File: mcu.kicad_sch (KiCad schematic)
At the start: 65 parts, among them J1 USB_C, P20 HEADER-2x11, P22 HEADER-2x13, P26 LPC_JTAG, P28 HEADER-2x11, SW1 SWITCH, SW2 SWITCH, U15 TVS_USB, U20 W25Q80, U23 LPC4330FET180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

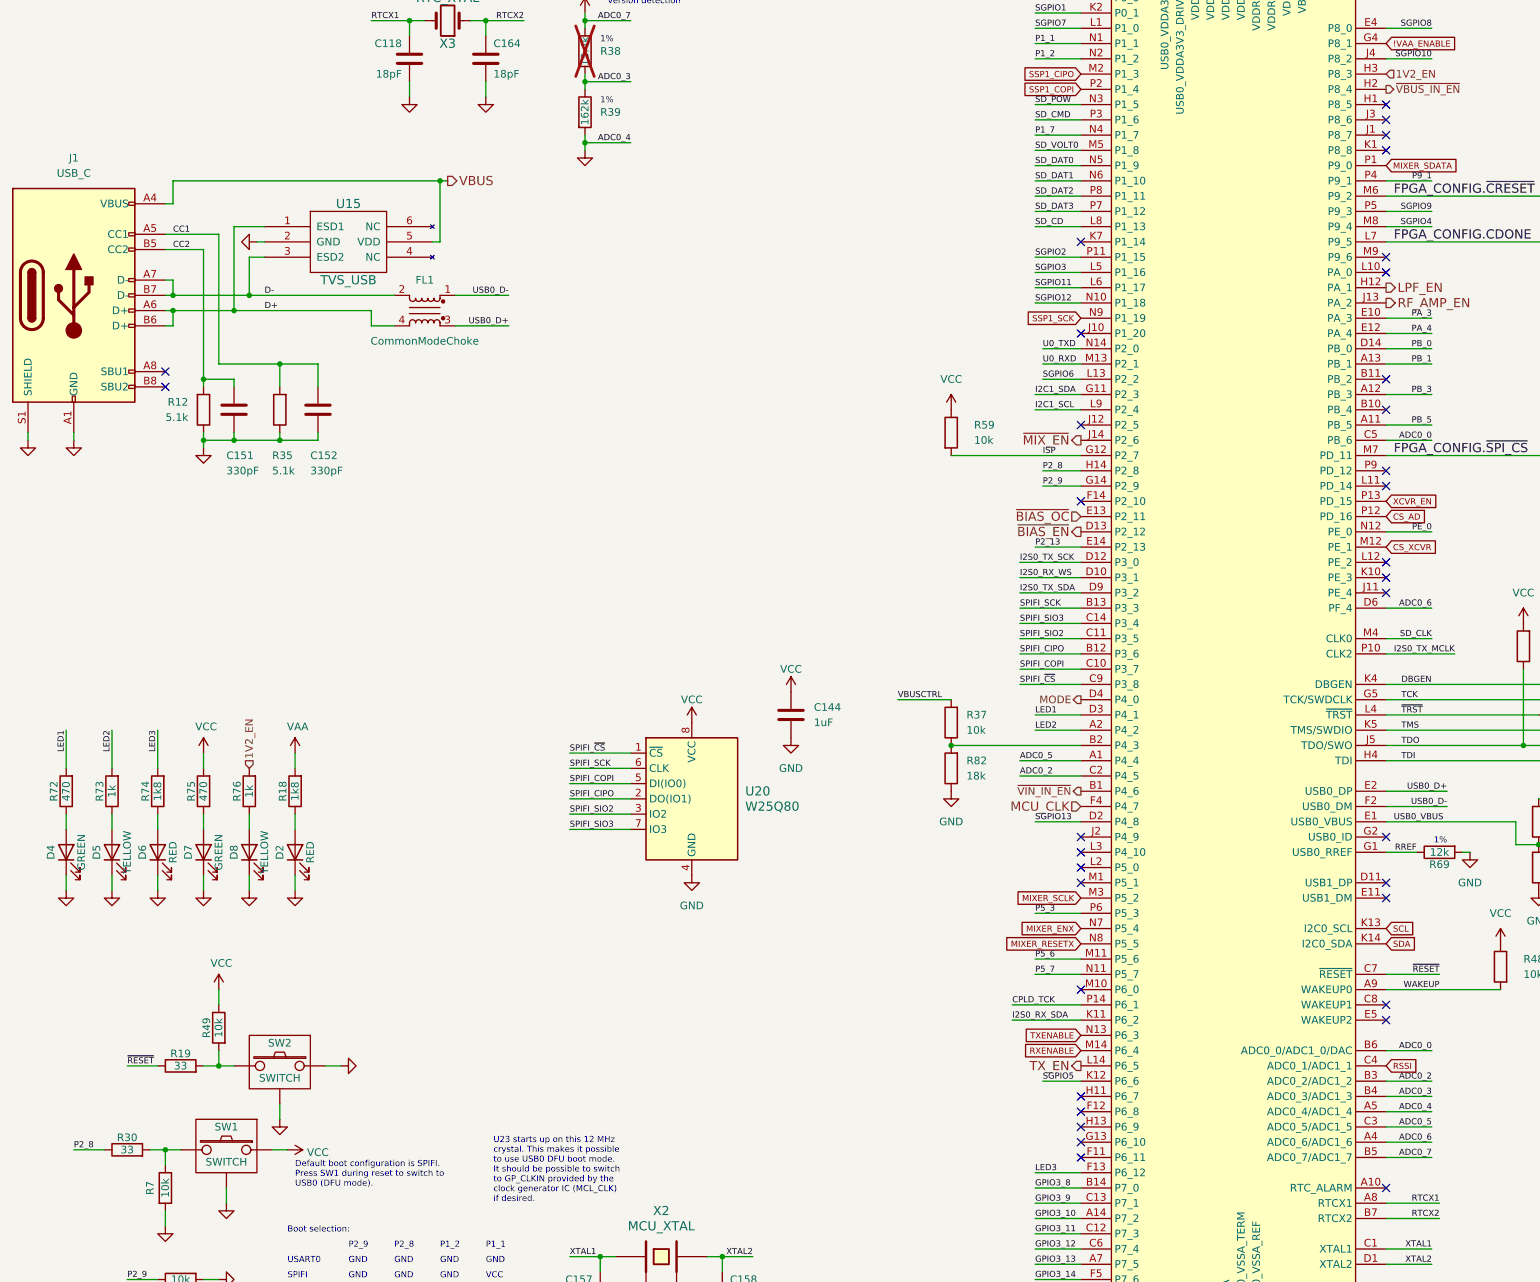
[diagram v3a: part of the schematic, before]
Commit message: Ensure LEDs can remain off in low power modes
- Change "3V3" LED to "MCU" LED4
- Change "1V2" LED to "FPGA" on 3V3FPGA
- Make LED control signals active-low
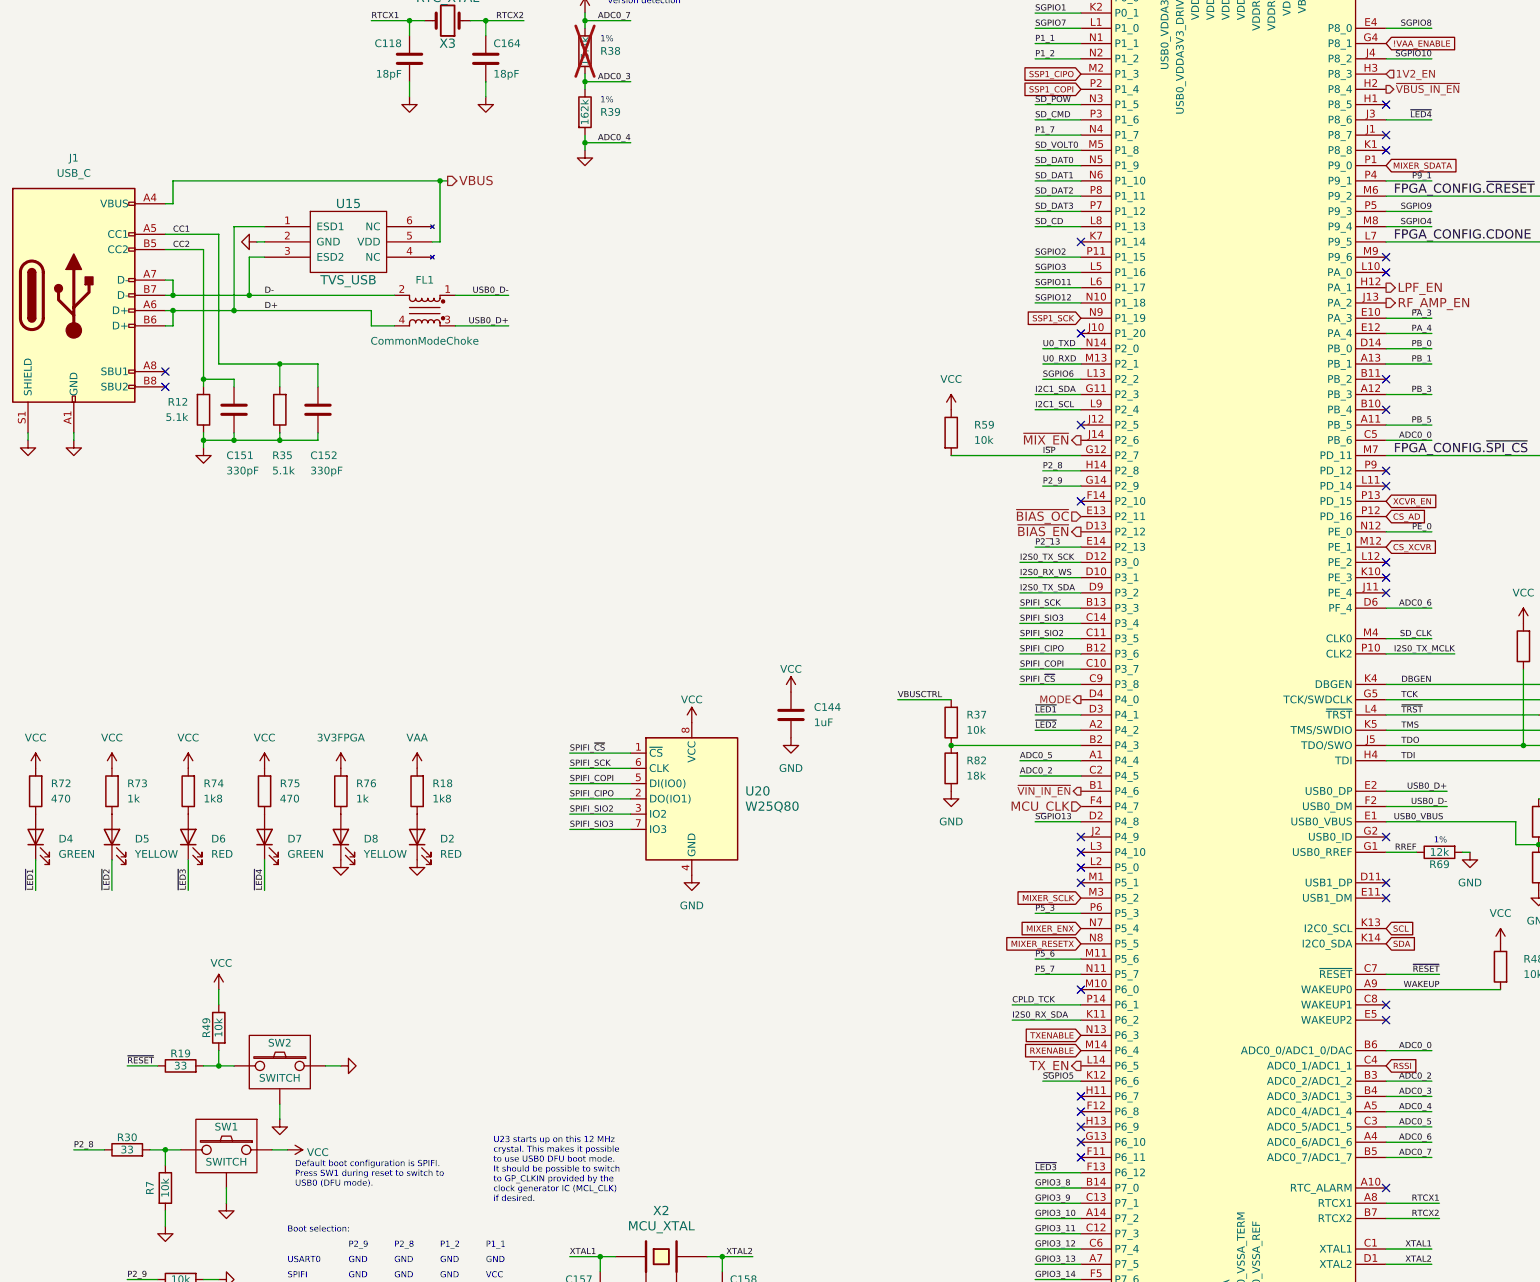
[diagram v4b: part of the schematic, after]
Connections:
- net 1V2_EN: no longer R76.2
- net GND: no longer D4.1 (K), D5.1 (K), D6.1 (K), D7.1 (K)
- net VCC: now also R72.2, R73.2, R74.2
- net ~{LED4}: now reaches U23.J3 (P8_6)
- net ~{LED4}: now also D7.1 (K)
- net LED1 renamed ~{LED1}
- net ~{LED1}: now also D4.1 (K); no longer R72.2
- net LED2 renamed ~{LED2}
- net ~{LED2}: now also D5.1 (K); no longer R73.2
- net LED3 renamed ~{LED3}
- net ~{LED3}: now also D6.1 (K); no longer R74.2
- new net 3V3FPGA: R76.2
- no-connect marks 37 -> 36
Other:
- moved on the sheet: D2, D4, D5, D6, D7, D8, R18, R72, R74, R75, R76
